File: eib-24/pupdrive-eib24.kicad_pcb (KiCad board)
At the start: 2 copper layers, 7.5 x 5.2 mm, 27 parts, among them J1 050702422

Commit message: Archive work before moving to leaf-spring design
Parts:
- moved J1 0.11 mm to (134.7, 129.7)
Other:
- outline, holes or cut-outs redrawn

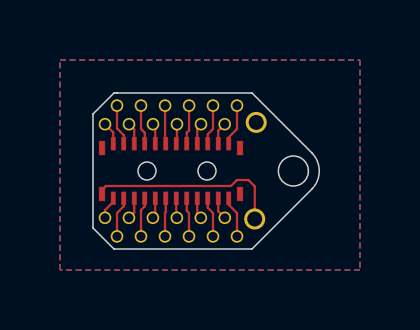
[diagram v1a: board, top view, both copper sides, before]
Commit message: Make eib-24 smaller to fit leaf-spring drive
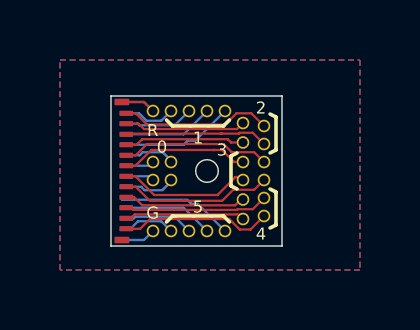
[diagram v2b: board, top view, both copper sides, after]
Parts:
- added J2: 050702422, jonnew:MOLEX_5050702422, B.Cu at (132.3, 129.7)
- TP26, TP4: footprint jonnew:NEURALYNX_LARGE-GOLD-PIN -> jonnew:NEURALYNX_SMALL-GOLD-PIN
- moved TP5 5.30 mm to (137.8, 131.2), turned to 90 degrees
- moved TP8 5.03 mm to (136.5, 131.7)
- moved TP26 4.99 mm to (134.1, 131.7)
- moved TP4 4.94 mm to (134.1, 127.7)
- moved TP2 4.82 mm to (135.3, 131.7)
- moved TP7 4.55 mm to (137.8, 130.6), turned to 90 degrees
- moved TP3 4.41 mm to (135.9, 131.7)
- moved TP6 4.24 mm to (137.1, 131.3), turned to 90 degrees
- moved TP1 4.18 mm to (134.7, 131.7)
- moved TP11 3.91 mm to (137.8, 130.0)
- moved TP25 3.79 mm to (137.8, 128.2)
- moved TP9 3.62 mm to (137.1, 130.7)
- moved TP17 3.52 mm to (137.8, 129.4)
- moved TP21 3.52 mm to (137.8, 128.8)
- moved TP23 3.22 mm to (137.1, 128.1)
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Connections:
- J1 pad MP1: /REF -> GNDA
- J1 pad MP3: unconnected-(J1-PadMP3) -> /REF
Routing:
- net /E5: track 0.67 -> 5.07 mm
- net /REF: track 6.55 -> 2.32 mm
- net /E1: track 0.75 -> 4.91 mm
- net /E3: track 0.71 -> 4.63 mm
- net /E7: track 0.65 -> 4.36 mm
- net /E8: track 1.29 -> 4.99 mm
- net /E12: track 1.37 -> 5.08 mm
- net /E10: track 1.33 -> 4.81 mm
- net /E9: track 0.69 -> 4.01 mm
- net /E11: track 0.73 -> 4.05 mm
- net /E6: track 1.27 -> 4.40 mm
- net /E21: track 0.71 -> 3.76 mm
- net /E4: track 1.31 -> 4.15 mm
- net /E16: track 1.33 -> 3.87 mm
- net /E2: track 1.35 -> 3.81 mm
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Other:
- board size 7.5 x 5.2 mm -> 5.7 x 5 mm
- board text added: "0"
- board text added: "1"
- board text added: "2"
- board text added: "3"
- board text added: "4"
- board text added: "5"
- board text added: "G"
- board text added: "R"

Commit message: Flex connector and eib-24 complete
- I need to panelize these and make different variants of the flex
connector with different lengths.
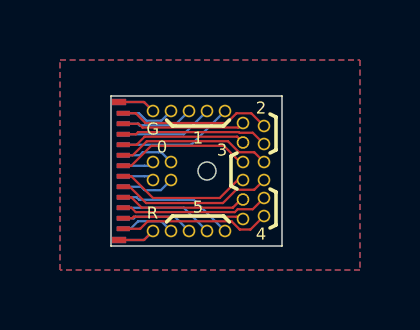
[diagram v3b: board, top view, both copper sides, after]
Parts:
- moved TP26 4.00 mm to (134.1, 127.7)
- moved TP4 4.00 mm to (134.1, 131.7)
- moved J1 0.10 mm to (132.2, 129.7)
- moved J2 0.10 mm to (132.2, 129.7)
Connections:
- J1 pad MP1: GNDA -> /REF
- J1 pad MP3: /REF -> GNDA
- J2 pad MP1: /REF -> GNDA
- J2 pad MP3: GNDA -> /REF
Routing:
- net GNDA: track 1.16 -> 2.52 mm
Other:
- outline, holes or cut-outs redrawn
- board text added: "Drive Edge"
